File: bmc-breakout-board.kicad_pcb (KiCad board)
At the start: 4 copper layers, 90 x 60 mm, 30 parts, among them J1 PinHeader_2x4, J10 PinHeader_2x4, J11 PinHeader_2x05, J12 61300411121, J14 PCIE_BUS_x1, J15 0473460001, J16 PinHeader_1x07, J17 UE27AC54100, J2 PinHeader_2x13, J3 PinHeader_2x08, J4 61300411121, J5 ME1016813401101, J6 61300411121, J7 DC_SOCKET, J8 PinHeader_2x05, J9 PinHeader_1x07, Q1 BSS138AKA

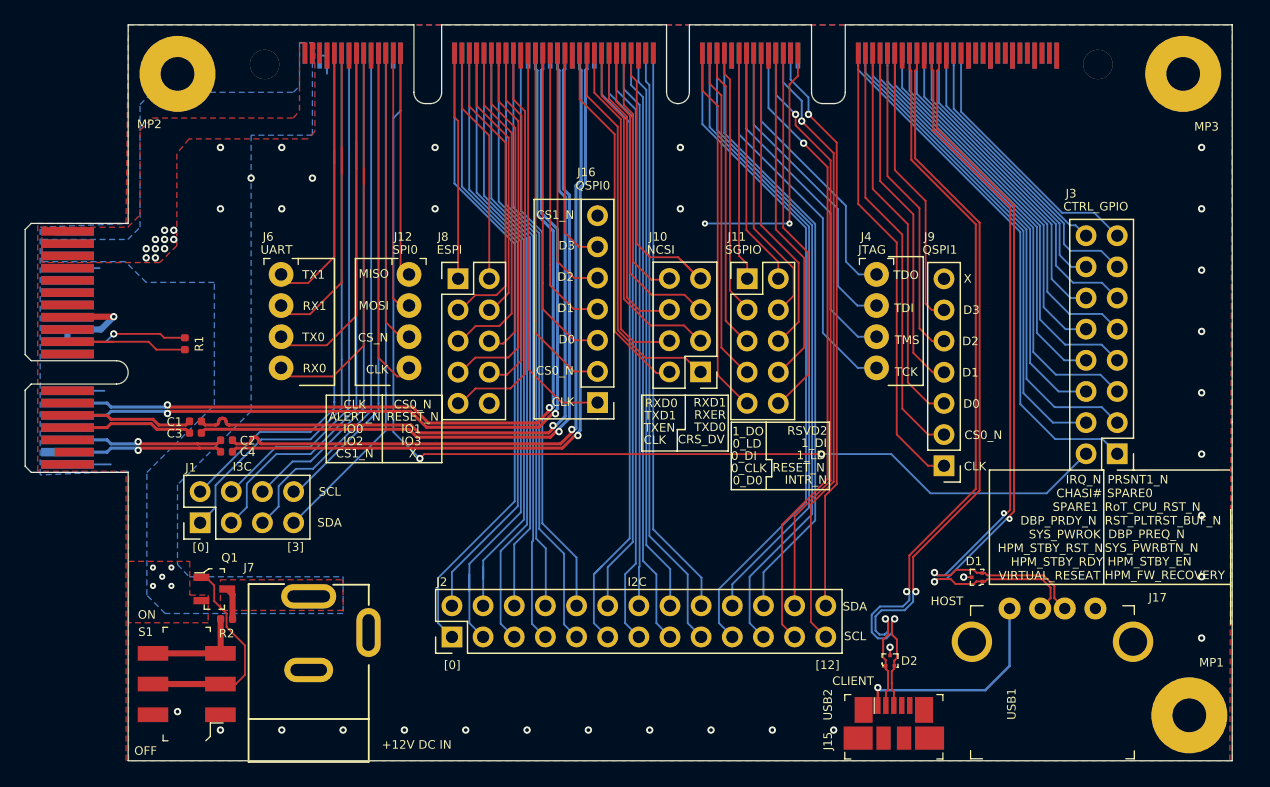
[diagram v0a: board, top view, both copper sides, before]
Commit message: Add GND probes
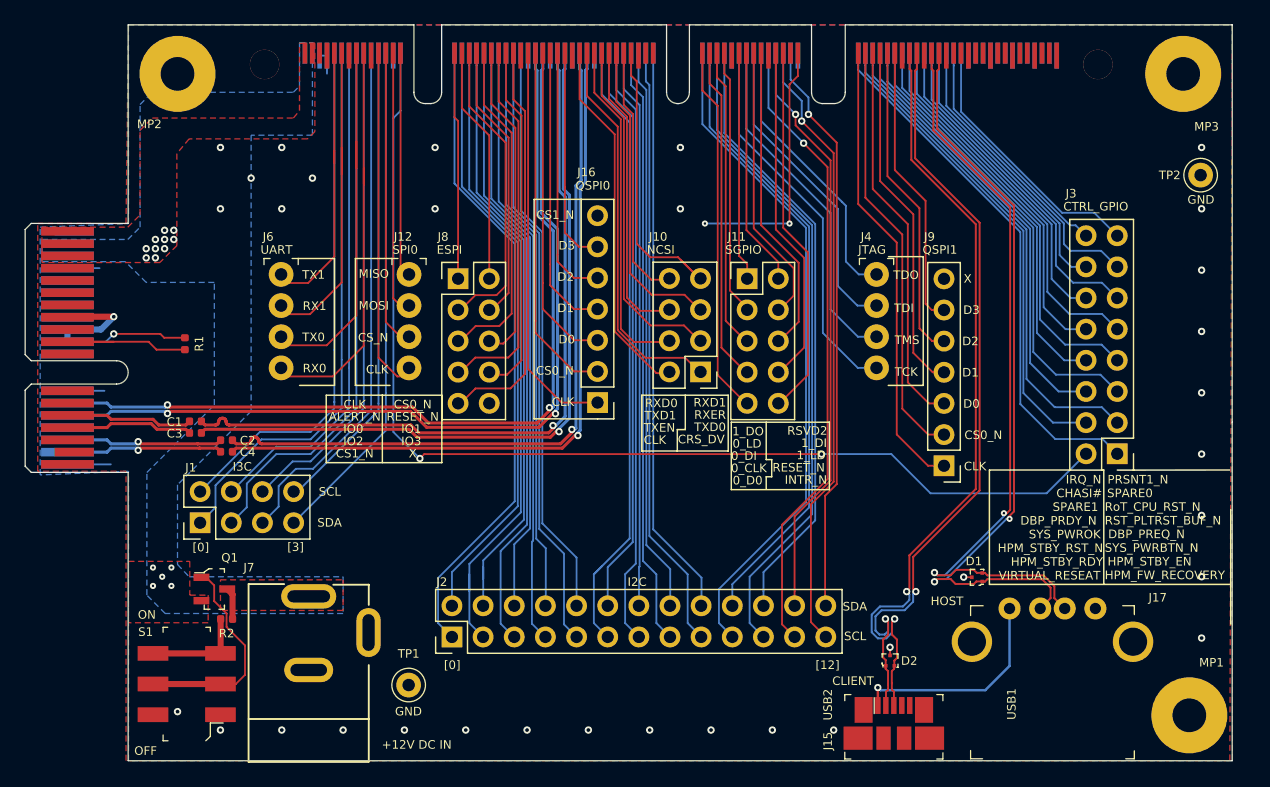
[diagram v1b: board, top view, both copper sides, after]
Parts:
- added TP1: 5001, bmc-breakout-board-footprints:Test_Point_D1.02mm, F.Cu at (82.9, 116.5)
- added TP2: 5001, bmc-breakout-board-footprints:Test_Point_D1.02mm, F.Cu at (147.5, 74.9)
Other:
- board text added: "GND"
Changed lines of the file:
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@@
   (general
     (thickness 1.55)
-    (drawings 236)
+    (drawings 238)
     (tracks 965)
     (zones 0)
-    (modules 30)
+    (modules 32)
     (nets 162)
   )
@@
     (add_net USB2_D_P)
   )
+  (module bmc-breakout-board-footprints:Test_Point_D1.02mm (layer F.Cu)
+    (at 147.52 74.92 180)
+    (attr virtual)
+    (fp_text reference TP2 (at 2.52 -0.005) (layer F.SilkS)
+      (effects (font (size 0.7 0.7) (thickness 0.15)))
+    )
+    (fp_text value 5001 (at 0 3.93) (layer F.Fab)
+      (effects (font (size 1 1) (thickness 0.15)))
+    )
+    (fp_text user %R (at 0 2.41) (layer F.Fab)
+      (effects (font (size 1 1) (thickness 0.15)))
+    )
+    (fp_circle (center 0 0) (end 1.52 0) (layer F.CrtYd) (width 0.05))
+    (fp_circle (center 0 0) (end 1.37 0) (layer F.SilkS) (width 0.1))
+    (fp_circle (center 0 0) (end 1.27 0) (layer F.Fab) (width 0.1))
+    (pad 1 thru_hole circle (at 0 0 180) (size 2.02 2.02) (drill 1.02) (layers *.Cu *.Mask)
+      (net 1 GND))
+  )
+  (module bmc-breakout-board-footprints:Test_Point_D1.02mm (layer F.Cu)
+    (at 82.945 116.495)
+    (attr virtual)
+    (fp_text reference TP1 (at 0 -2.55) (layer F.SilkS)
+      (effects (font (size 0.7 0.7) (thickness 0.15)))
+    )
+    (fp_text value 5001 (at 0 3.93) (layer F.Fab)
+      (effects (font (size 1 1) (thickness 0.15)))
+    )
+    (fp_text user %R (at 0 2.41) (layer F.Fab)
+      (effects (font (size 1 1) (thickness 0.15)))
+    )
+    (fp_circle (center 0 0) (end 1.52 0) (layer F.CrtYd) (width 0.05))
+    (fp_circle (center 0 0) (end 1.37 0) (layer F.SilkS) (width 0.1))
+    (fp_circle (center 0 0) (end 1.27 0) (layer F.Fab) (width 0.1))
+    (pad 1 thru_hole circle (at 0 0) (size 2.02 2.02) (drill 1.02) (layers *.Cu *.Mask)
+      (net 1 GND))
+  )
   (module bmc-breakout-board-footprints:0402-cap (layer F.Cu)
     (at 68.095 97.475 180)
@@
     )
   )
+  (gr_text GND (at 147.545 76.925) (layer F.SilkS)
+    (effects (font (size 0.7 0.7) (thickness 0.15)))
+  )
+  (gr_text GND (at 82.93 118.65) (layer F.SilkS)
+    (effects (font (size 0.7 0.7) (thickness 0.15)))
+  )
   (gr_text HOST (at 126.84 109.655) (layer F.SilkS)

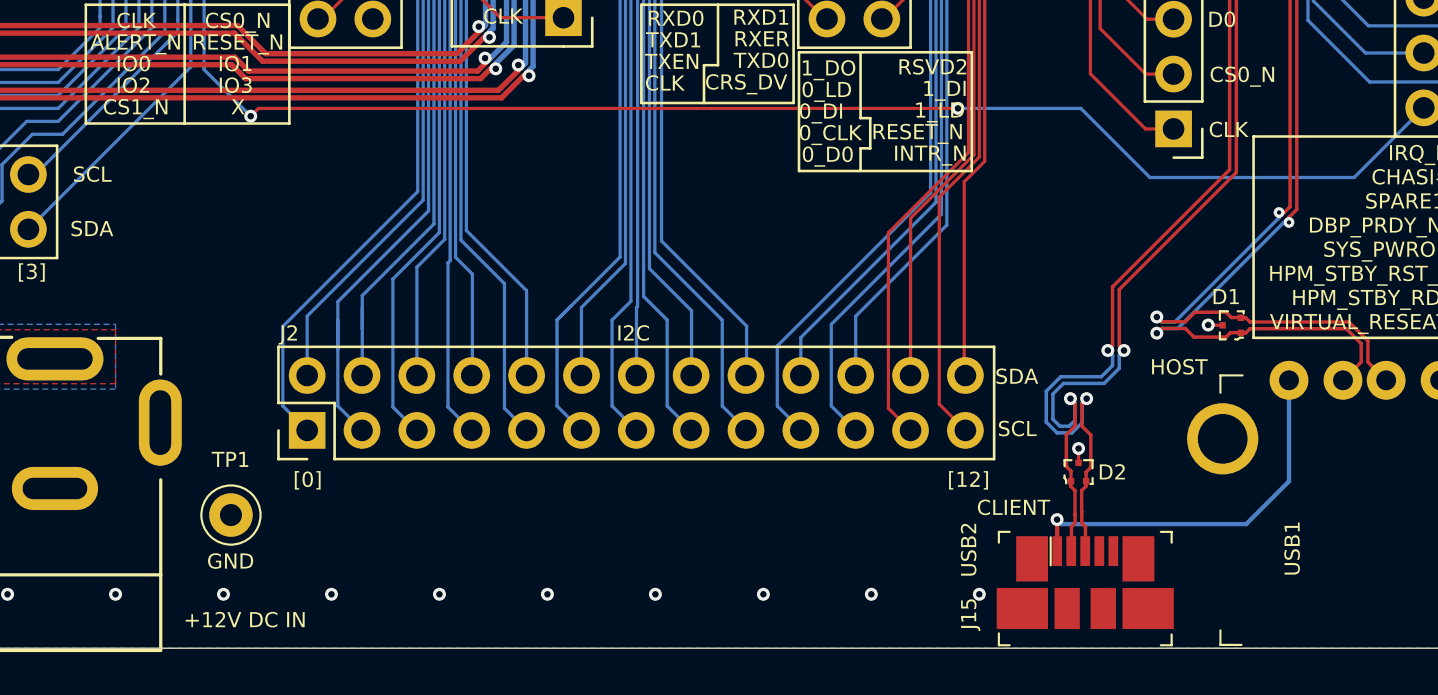
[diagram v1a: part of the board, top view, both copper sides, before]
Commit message: Add FTDI circuit on PCB and do routing
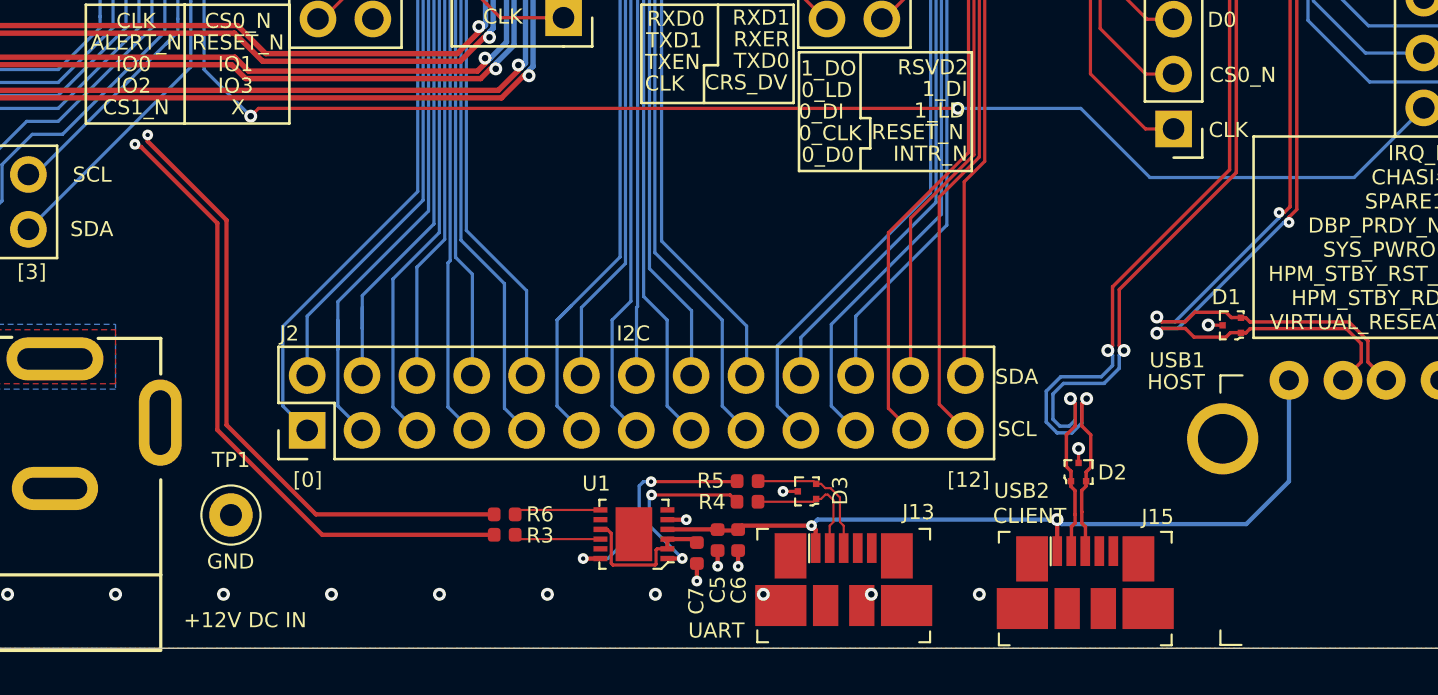
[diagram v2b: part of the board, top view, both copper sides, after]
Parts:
- added C5: C_100n_0402, bmc-breakout-board-footprints:0402-cap, F.Cu at (105.5, 117.7)
- added C6: C_1u_0402, bmc-breakout-board-footprints:0402-cap, F.Cu at (106.4, 117.7)
- added C7: C_100n_0402, bmc-breakout-board-footprints:0402-cap, F.Cu at (104.5, 118.3)
- added D3: TPD2E009, bmc-breakout-board-footprints:SOT-3, F.Cu at (109.6, 115.4)
- added J13: 0473460001, bmc-breakout-board-footprints:USB_Micro_B_Female_0473460001, F.Cu at (111.3, 120.7)
- added R3: R_220R_0402, bmc-breakout-board-footprints:0402-res, F.Cu at (95.6, 117.4)
- added R4: R_22R_0402, bmc-breakout-board-footprints:0402-res, F.Cu at (106.9, 115.9)
- added R5: R_22R_0402, bmc-breakout-board-footprints:0402-res, F.Cu at (106.9, 114.9)
- added R6: R_220R_0402, bmc-breakout-board-footprints:0402-res, F.Cu at (95.6, 116.5)
- added U1: FT234XD-R, bmc-breakout-board-footprints:DFN-12-1EP_3x3mm, F.Cu at (101.6, 117.4)
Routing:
- net UART0_SCM_TX: track 30.7 -> 76.2 mm, vias 0 -> 1
- net UART0_SCM_RX: track 32.9 -> 73.1 mm, vias 0 -> 1
- net VBUS: track 17.7 -> 37.0 mm, vias 1 -> 2
- net Net-(R5-Pad2): track 0.00 -> 10.7 mm, vias 0 -> 2
- net Net-(R4-Pad2): track 0.00 -> 8.40 mm, vias 0 -> 2
- net Net-(C7-Pad2): track 0.00 -> 7.18 mm
- net FTDI_USB_D_P: track 0.00 -> 6.45 mm
- net FTDI_USB_D_N: track 0.00 -> 5.96 mm
- net /UART_TX: track 0.00 -> 4.04 mm
- net /UART_RX: track 0.00 -> 4.02 mm
- net GND: track 15.8 -> 19.6 mm, vias 30 -> 35

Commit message: Change power switch
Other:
- board text added: "DC-SCM Breakout Board Rev. 1.0.0"
- board text removed: "BMC Breakout Docker Board Rev. 1.0.0"
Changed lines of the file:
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@@
-(kicad_pcb (version 20171130) (host pcbnew 5.1.9+dfsg1-1~bpo10+1)
+(kicad_pcb (version 20171130) (host pcbnew 5.1.5+dfsg1-2~bpo10+1)
   (general
     (thickness 1.55)
@@
   (page A4)
   (layers
-    (0 F.Cu signal)
-    (1 In1.Cu power)
+    (0 F.Cu signal hide)
+    (1 In1.Cu power hide)
     (2 In2.Cu power hide)
-    (31 B.Cu signal)
-    (32 B.Adhes user)
-    (33 F.Adhes user)
-    (34 B.Paste user)
-    (35 F.Paste user)
-    (36 B.SilkS user)
-    (37 F.SilkS user)
-    (38 B.Mask user)
+    (31 B.Cu signal hide)
+    (32 B.Adhes user hide)
+    (33 F.Adhes user hide)
+    (34 B.Paste user hide)
+    (35 F.Paste user hide)
+    (36 B.SilkS user hide)
+    (37 F.SilkS user hide)
+    (38 B.Mask user hide)
     (39 F.Mask user)
-    (40 Dwgs.User user)
-    (41 Cmts.User user)
-    (42 Eco1.User user)
-    (43 Eco2.User user)
-    (44 Edge.Cuts user)
-    (45 Margin user)
-    (46 B.CrtYd user)
+    (40 Dwgs.User user hide)
+    (41 Cmts.User user hide)
+    (42 Eco1.User user hide)
+    (43 Eco2.User user hide)
+    (44 Edge.Cuts user hide)
+    (45 Margin user hide)
+    (46 B.CrtYd user hide)
     (47 F.CrtYd user)
-    (48 B.Fab user)
+    (48 B.Fab user hide)
     (49 F.Fab user hide)
   )
   (setup
-    (last_trace_width 0.15)
+    (last_trace_width 0.1)
     (user_trace_width 0.15)
     (user_trace_width 0.2)
@@
     (effects (font (size 1.5 1.5) (thickness 0.3)) (justify left))
   )
-  (gr_text "BMC Breakout Docker Board\nRev. 1.0.0" (at 90.535 105.45) (layer F.Mask)
+  (gr_text "DC-SCM Breakout Board\nRev. 1.0.0" (at 90.535 105.45) (layer F.Mask)
     (effects (font (size 1 1) (thickness 0.2)) (justify left))
   )
@@
   (segment (start 58.350001 94.505) (end 58.675001 94.83) (width 0.25) (layer F.Cu) (net 120))
   (segment (start 58.675001 94.83) (end 62.102488 94.83) (width 0.25) (layer F.Cu) (net 120))
-  (via (at 95.207488 95.832488) (size 0.6) (drill 0.3) (layers F.Cu B.Cu) (net 161))
-  (segment (start 95.207488 95.585) (end 96.055 94.737488) (width 0.25) (layer B.Cu) (net 161))
-  (segment (start 95.207488 95.832488) (end 95.207488 95.585) (width 0.25) (layer B.Cu) (net 161))
-  (segment (start 96.055 94.737488) (end 96.055 76.542512) (width 0.25) (layer B.Cu) (net 161))
-  (segment (start 96.055 76.542512) (end 95.56 76.047512) (width 0.25) (layer B.Cu) (net 161))
-  (segment (start 95.705 94.592512) (end 95.705 76.687488) (width 0.25) (layer B.Cu) (net 159))
-  (segment (start 94.96 95.337512) (end 95.705 94.592512) (width 0.25) (layer B.Cu) (net 159))
-  (segment (start 94.712512 95.337512) (end 94.96 95.337512) (width 0.25) (layer B.Cu) (net 159))
-  (segment (start 95.705 76.687488) (end 95.21 76.192488) (width 0.25) (layer B.Cu) (net 159))
-  (via (at 94.712512 95.337512) (size 0.6) (drill 0.3) (layers F.Cu B.Cu) (net 159))
   (segment (start 55.125 93.505) (end 58.350001 93.505) (width 0.25) (layer B.Cu) (net 121))
   (segment (start 58.350001 93.505) (end 58.675001 93.83) (width 0.25) (layer B.Cu) (net 121))
@@
   (segment (start 55.125 96.505) (end 58.350001 96.505) (width 0.25) (layer B.Cu) (net 123))
   (segment (start 58.350001 96.505) (end 58.675001 96.83) (width 0.25) (layer B.Cu) (net 123))
-  (via (at 96.252512 95.657512) (size 0.6) (drill 0.3) (layers F.Cu B.Cu) (net 160))
   (via (at 60.89 96.655) (size 0.6) (drill 0.3) (layers F.Cu B.Cu) (net 123))
   (segment (start 60.715 96.83) (end 60.89 96.655) (width 0.25) (layer B.Cu) (net 123))
@@
   (segment (start 58.350001 97.505) (end 58.675001 97.18) (width 0.25) (layer B.Cu) (net 124))
   (segment (start 55.125 97.505) (end 58.350001 97.505) (width 0.25) (layer B.Cu) (net 124))
-  (via (at 96.747488 96.152488) (size 0.6) (drill 0.3) (layers F.Cu B.Cu) (net 162))
   (segment (start 60.715 97.18) (end 60.89 97.355) (width 0.25) (layer B.Cu) (net 124))
   (segment (start 58.675001 97.18) (end 60.715 97.18) (width 0.25) (layer B.Cu) (net 124))
@@
   (segment (start 67.615 113.9) (end 67.6 113.915) (width 0.5) (layer F.Cu) (net 157))
   (segment (start 67.615 111.115) (end 67.615 113.9) (width 0.5) (layer F.Cu) (net 157))
+  (segment (start 95.705 94.592512) (end 95.705 76.687488) (width 0.25) (layer B.Cu) (net 159))
+  (segment (start 94.96 95.337512) (end 95.705 94.592512) (width 0.25) (layer B.Cu) (net 159))
+  (segment (start 94.712512 95.337512) (end 94.96 95.337512) (width 0.25) (layer B.Cu) (net 159))
+  (segment (start 95.705 76.687488) (end 95.21 76.192488) (width 0.25) (layer B.Cu) (net 159))
+  (via (at 94.712512 95.337512) (size 0.6) (drill 0.3) (layers F.Cu B.Cu) (net 159))
   (segment (start 95.21 66.390001) (end 95.085 66.265001) (width 0.25) (layer B.Cu) (net 159))
   (segment (start 95.085 66.265001) (end 95.085 64.975) (width 0.25) (layer B.Cu) (net 159))
-  (segment (start 95.56 66.390001) (end 95.685 66.265001) (width 0.25) (layer B.Cu) (net 161))
-  (segment (start 95.685 66.265001) (end 95.685 64.975) (width 0.25) (layer B.Cu) (net 161))
-  (segment (start 95.56 76.047512) (end 95.56 66.390001) (width 0.25) (layer B.Cu) (net 161))
   (segment (start 95.21 76.192488) (end 95.21 66.390001) (width 0.25) (layer B.Cu) (net 159))
   (segment (start 94.362512 95.935) (end 94.712512 95.585) (width 0.25) (layer F.Cu) (net 159))
@@
   (segment (start 67.243632 95.285612) (end 67.3017 95.265294) (width 0.25) (layer F.Cu) (net 159))
   (segment (start 67.731958 94.743042) (end 67.7825 94.743042) (width 0.25) (layer F.Cu) (net 159))
+  (via (at 96.252512 95.657512) (size 0.6) (drill 0.3) (layers F.Cu B.Cu) (net 160))
   (segment (start 96.5 95.657512) (end 96.585 95.572512) (width 0.25) (layer B.Cu) (net 160))
   (segment (start 96.252512 95.657512) (end 96.5 95.657512) (width 0.25) (layer B.Cu) (net 160))
   (segment (start 96.585 75.772512) (end 97.01 75.347512) (width 0.25) (layer B.Cu) (net 160))
   (segment (start 96.585 95.572512) (end 96.585 75.772512) (width 0.25) (layer B.Cu) (net 160))
-  (segment (start 96.747488 95.905) (end 96.935 95.717488) (width 0.25) (layer B.Cu) (net 162))
-  (segment (start 96.747488 96.152488) (end 96.747488 95.905) (width 0.25) (layer B.Cu) (net 162))
-  (segment (start 96.935 95.717488) (end 96.935 75.917488) (width 0.25) (layer B.Cu) (net 162))
-  (segment (start 96.935 75.917488) (end 97.36 75.492488) (width 0.25) (layer B.Cu) (net 162))
   (segment (start 97.01 66.390001) (end 96.885 66.265001) (width 0.25) (layer B.Cu) (net 160))
   (segment (start 96.885 66.265001) (end 96.885 64.975) (width 0.25) (layer B.Cu) (net 160))
@@
   (segment (start 70.971958 96.8275) (end 95.330012 96.8275) (width 0.25) (layer F.Cu) (net 160))
   (segment (start 96.252512 95.905) (end 96.252512 95.657512) (width 0.25) (layer F.Cu) (net 160))
+  (via (at 95.207488 95.832488) (size 0.6) (drill 0.3) (layers F.Cu B.Cu) (net 161))
+  (segment (start 95.207488 95.585) (end 96.055 94.737488) (width 0.25) (layer B.Cu) (net 161))
+  (segment (start 95.207488 95.832488) (end 95.207488 95.585) (width 0.25) (layer B.Cu) (net 161))
+  (segment (start 96.055 94.737488) (end 96.055 76.542512) (width 0.25) (layer B.Cu) (net 161))
+  (segment (start 96.055 76.542512) (end 95.56 76.047512) (width 0.25) (layer B.Cu) (net 161))
+  (segment (start 95.56 66.390001) (end 95.685 66.265001) (width 0.25) (layer B.Cu) (net 161))
+  (segment (start 95.685 66.265001) (end 95.685 64.975) (width 0.25) (layer B.Cu) (net 161))
+  (segment (start 95.56 76.047512) (end 95.56 66.390001) (width 0.25) (layer B.Cu) (net 161))
   (segment (start 82.980012 95.6425) (end 83.622512 96.285) (width 0.25) (layer F.Cu) (net 161))
   (segment (start 66.3425 95.6425) (end 82.980012 95.6425) (width 0.25) (layer F.Cu) (net 161))
@@
   (segment (start 83.622512 96.285) (end 94.507488 96.285) (width 0.25) (layer F.Cu) (net 161))
   (segment (start 94.96 95.832488) (end 95.207488 95.832488) (width 0.25) (layer F.Cu) (net 161))
+  (via (at 96.747488 96.152488) (size 0.6) (drill 0.3) (layers F.Cu B.Cu) (net 162))
+  (segment (start 96.747488 95.905) (end 96.935 95.717488) (width 0.25) (layer B.Cu) (net 162))
+  (segment (start 96.747488 96.152488) (end 96.747488 95.905) (width 0.25) (layer B.Cu) (net 162))
+  (segment (start 96.935 95.717488) (end 96.935 75.917488) (width 0.25) (layer B.Cu) (net 162))
+  (segment (start 96.935 75.917488) (end 97.36 75.492488) (width 0.25) (layer B.Cu) (net 162))
   (segment (start 97.36 66.390001) (end 97.485 66.265001) (width 0.25) (layer B.Cu) (net 162))
   (segment (start 97.485 66.265001) (end 97.485 64.975) (width 0.25) (layer B.Cu) (net 162))
